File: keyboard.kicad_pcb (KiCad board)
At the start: 2 copper layers, 284.5 x 94 mm, 160 parts, among them J1 Conn_SWD, J2 Conn_ETM, J3 USB_C_Receptacle, J4 JST_PH, J5 PicoBlade, J6 PicoBlade, J7 2.54mm, J8 PicoBlade, J9 PicoBlade, Q2 FDC6312P, SW1 Slide Switch, U1 BL653, U2 BQ24295, U3 MCP73832-2-MC, U4 MCP1811AT-033/OT, Y1 32.768kHz

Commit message: archive footprints and schematics symbols
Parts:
- C1, C10, C11, C12, C13, C14, C15, C16, C17, C2, C3, C4, C5, C7, C8: footprint Capacitor_SMD:C_0805_2012Metric -> archive:C_0805_2012Metric
- C6, C9: footprint Capacitor_SMD:C_1206_3216Metric -> archive:C_1206_3216Metric
- D1, D10, D11, D12, D13, D14, D15, D16, D17, D18, D19, D2, D20, D21, D22, D23, D24, D25, D26, D27, D28, D29, D3, D30, D31, D32, D33, D4, D5, D6, D7, D8, D9: footprint Package_TO_SOT_SMD:SOT-23 -> archive:SOT-23
- D34, D35, D36: footprint Diode_SMD:D_SOD-123 -> archive:D_SOD-123
- F1: footprint Fuse:Fuseholder_Littelfuse_Nano2_154x -> archive:Fuseholder_Littelfuse_Nano2_154x
- J1: footprint Connector_PinHeader_1.27mm:PinHeader_2x05_P1.27mm_Vertical_SMD -> archive:PinHeader_2x05_P1.27mm_Vertical_SMD
- J2: footprint Connector_PinHeader_1.27mm:PinHeader_2x10_P1.27mm_Vertical_SMD -> archive:PinHeader_2x10_P1.27mm_Vertical_SMD
- J3: footprint Connector_USB:USB_C_Receptacle_HRO_TYPE-C-31-M-12 -> archive:USB_C_Receptacle_HRO_TYPE-C-31-M-12
- J4: footprint Connector_JST:JST_PH_S2B-PH-SM4-TB_1x02-1MP_P2.00mm_Horizontal -> archive:JST_PH_S2B-PH-SM4-TB_1x02-1MP_P2.00mm_Horizontal
- J5, J6, J8, J9: footprint Connector_Molex:Molex_PicoBlade_53261-0271_1x02-1MP_P1.25mm_Horizontal -> archive:Molex_PicoBlade_53261-0271_1x02-1MP_P1.25mm_Horizontal
- J7: footprint Connector_PinHeader_2.54mm:PinHeader_1x14_P2.54mm_Vertical -> archive:PinHeader_1x14_P2.54mm_Vertical
- JP100: footprint project:GND_Tie -> archive:GND_Tie
- L1: footprint Inductor_SMD:L_Bourns-SRN4018 -> archive:L_Bourns-SRN4018
- LED1, LED2: footprint LED_SMD:LED_0805_2012Metric -> archive:LED_0805_2012Metric
- LED3: footprint LED_THT:LED_D3.0mm -> archive:LED_D3.0mm
- MK1: footprint project:Hole_1 -> archive:Hole_1
- MK2, MK3, MK6: footprint project:Hole_2 -> archive:Hole_2
- MK4, MK5: footprint project:Hole_3 -> archive:Hole_3
- Q2: footprint Package_TO_SOT_SMD:SuperSOT-6 -> archive:SuperSOT-6
- R1, R10, R12, R13, R14, R15, R16, R2, R4, R5, R6, R7, R8, R9, TH1: footprint Resistor_SMD:R_0805_2012Metric -> archive:R_0805_2012Metric
- S1, S10, S11, S12, S13, S16, S17, S18, S19, S2, S20, S21, S22, S23, S24, S25, S26, S27, S3, S30, S31, S32, S33, S34, S35, S36, S37, S38, S39, S4, S40, S43, S44, S45, S46, S47, S48, S49, S5, S50, S51, S52, S53, S54, S55, S6, S60, S61, S62, S63, S64, S7, S8, S9: footprint Button_Switch_Keyboard:SW_Cherry_MX_1.00u_PCB -> archive:SW_Cherry_MX_1.00u_PCB
- S14, S42: footprint Button_Switch_Keyboard:SW_Cherry_MX_2.00u_PCB -> archive:SW_Cherry_MX_2.00u_PCB
- S15, S28: footprint Button_Switch_Keyboard:SW_Cherry_MX_1.50u_PCB -> archive:SW_Cherry_MX_1.50u_PCB
- S29: footprint Button_Switch_Keyboard:SW_Cherry_MX_1.75u_PCB -> archive:SW_Cherry_MX_1.75u_PCB
- S41: footprint Button_Switch_Keyboard:SW_Cherry_MX_2.25u_PCB -> archive:SW_Cherry_MX_2.25u_PCB
- S56, S57, S58: footprint Button_Switch_Keyboard:SW_Cherry_MX_1.25u_PCB -> archive:SW_Cherry_MX_1.25u_PCB
- S59: footprint Button_Switch_Keyboard:SW_Cherry_MX_6.25u_PCB -> archive:SW_Cherry_MX_6.25u_PCB
- SW1: footprint project:SW_OS102011MS2QN1 -> archive:SW_OS102011MS2QN1
- U1: footprint project:Laird_BL653 -> archive:Laird_BL653
- U2: footprint Package_DFN_QFN:QFN-24-1EP_4x4mm_P0.5mm_EP2.65x2.65mm -> archive:QFN-24-1EP_4x4mm_P0.5mm_EP2.65x2.65mm
- U3: footprint Package_DFN_QFN:DFN-8-1EP_3x2mm_P0.5mm_EP1.7x1.4mm -> archive:DFN-8-1EP_3x2mm_P0.5mm_EP1.7x1.4mm
- U4: footprint Package_TO_SOT_SMD:SOT-23-5 -> archive:SOT-23-5
- Y1: footprint Crystal:Crystal_SMD_3215-2Pin_3.2x1.5mm -> archive:Crystal_SMD_3215-2Pin_3.2x1.5mm

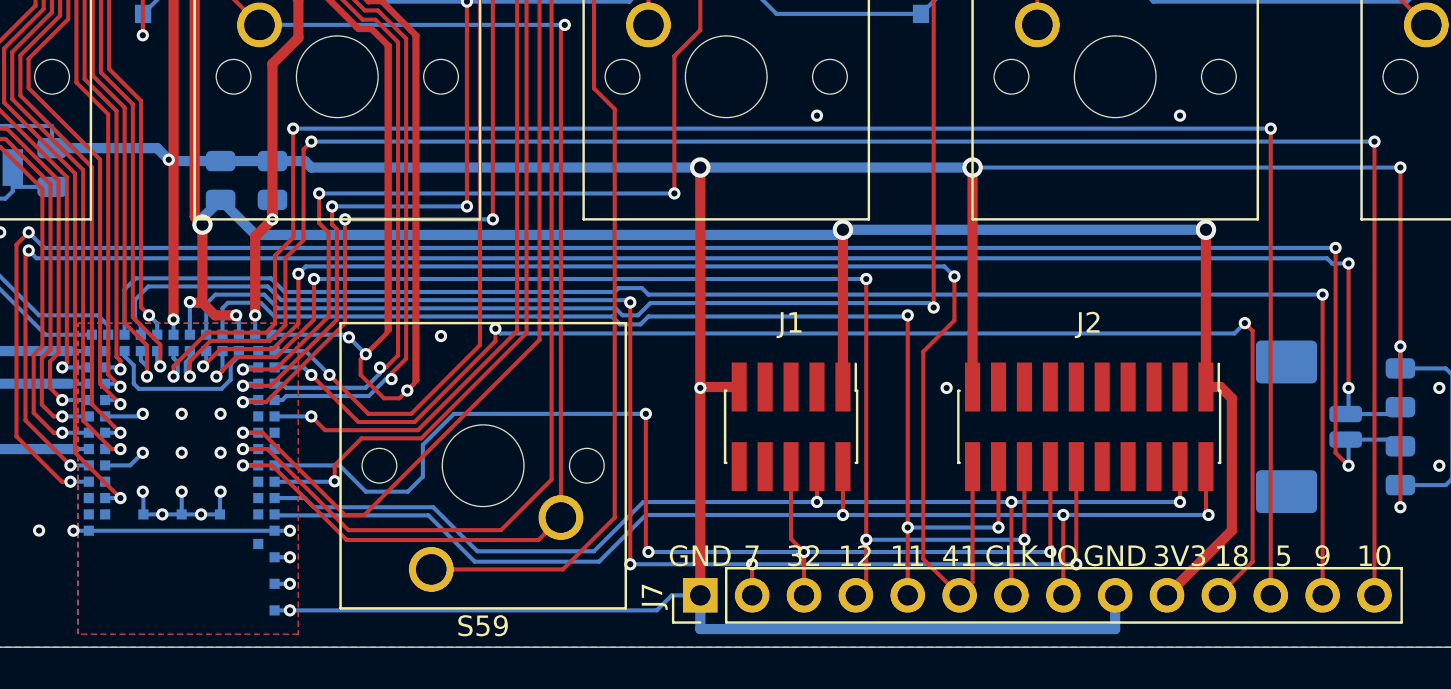
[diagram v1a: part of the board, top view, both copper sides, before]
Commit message: small change to expansion header pinout
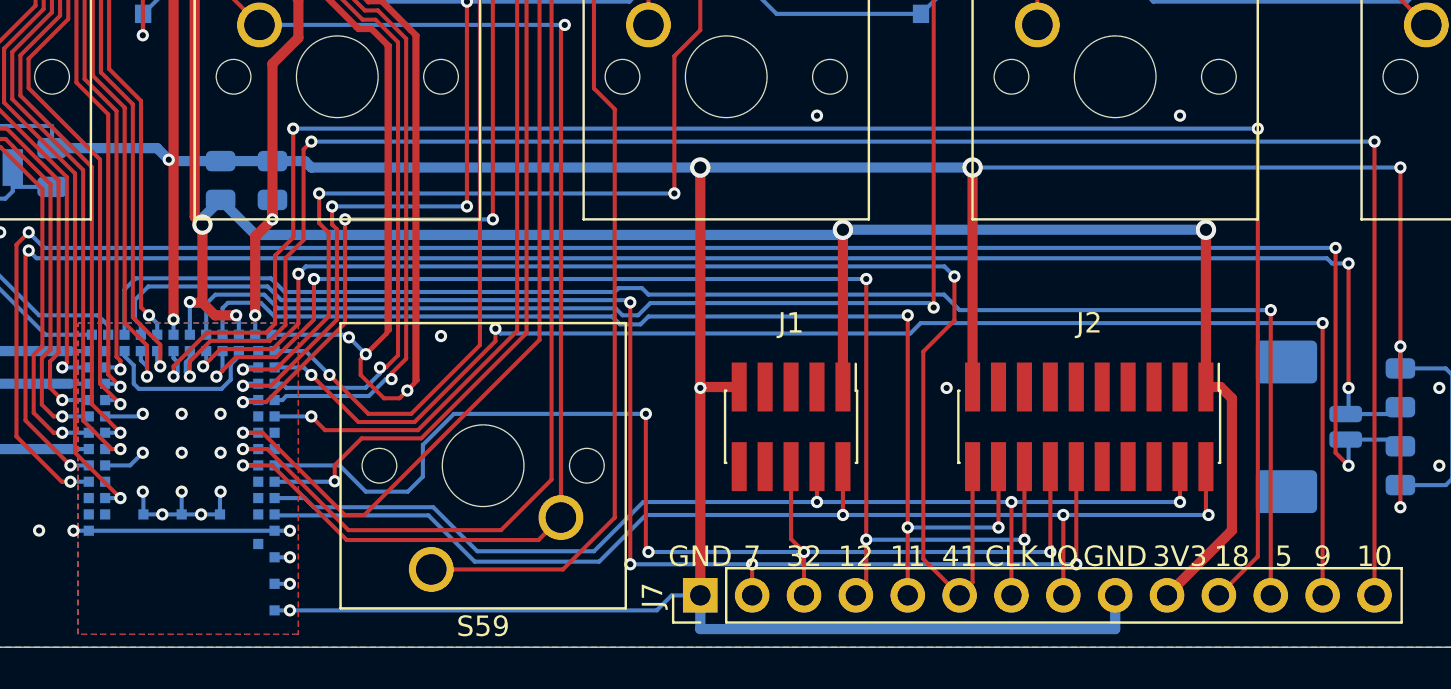
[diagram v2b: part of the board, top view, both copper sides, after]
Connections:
- J7 pad 11: /P18 -> /P4
- J7 pad 12: /P4 -> /P5
- J7 pad 13: /P5 -> /P18
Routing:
- net /P5: track 76.3 -> 73.4 mm
- net /P18: track 65.4 -> 68.3 mm
